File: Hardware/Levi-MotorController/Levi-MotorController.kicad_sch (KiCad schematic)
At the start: 3 parts

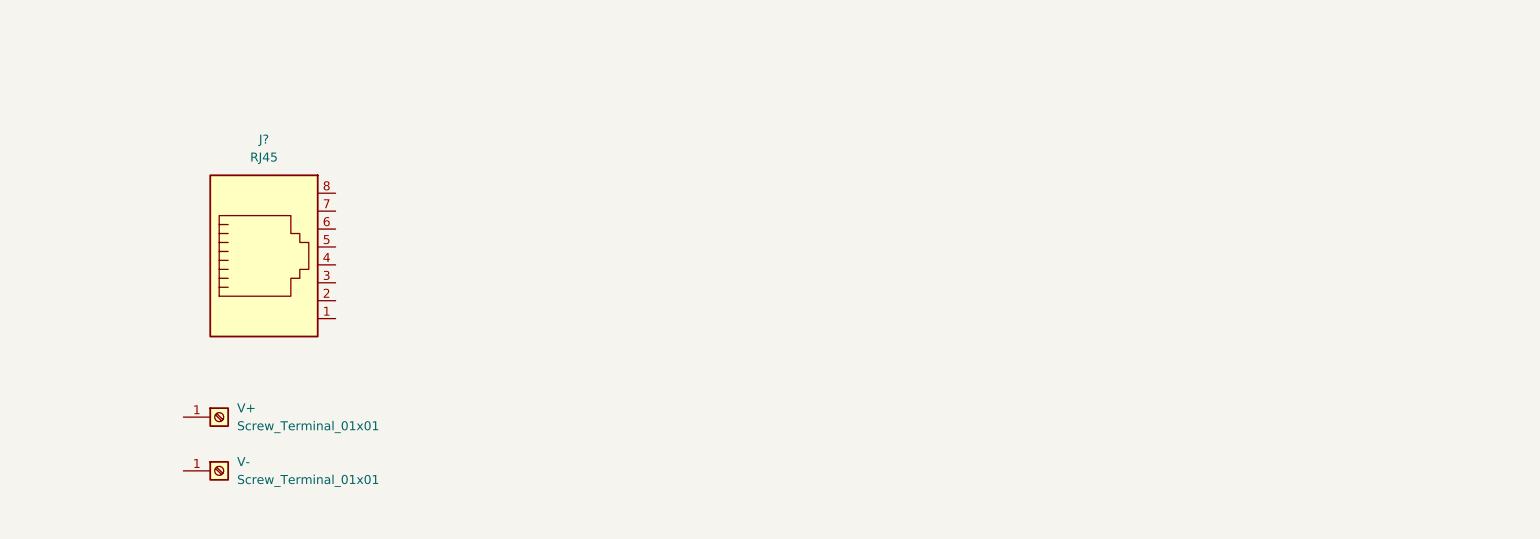
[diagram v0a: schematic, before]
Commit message: adding footprints
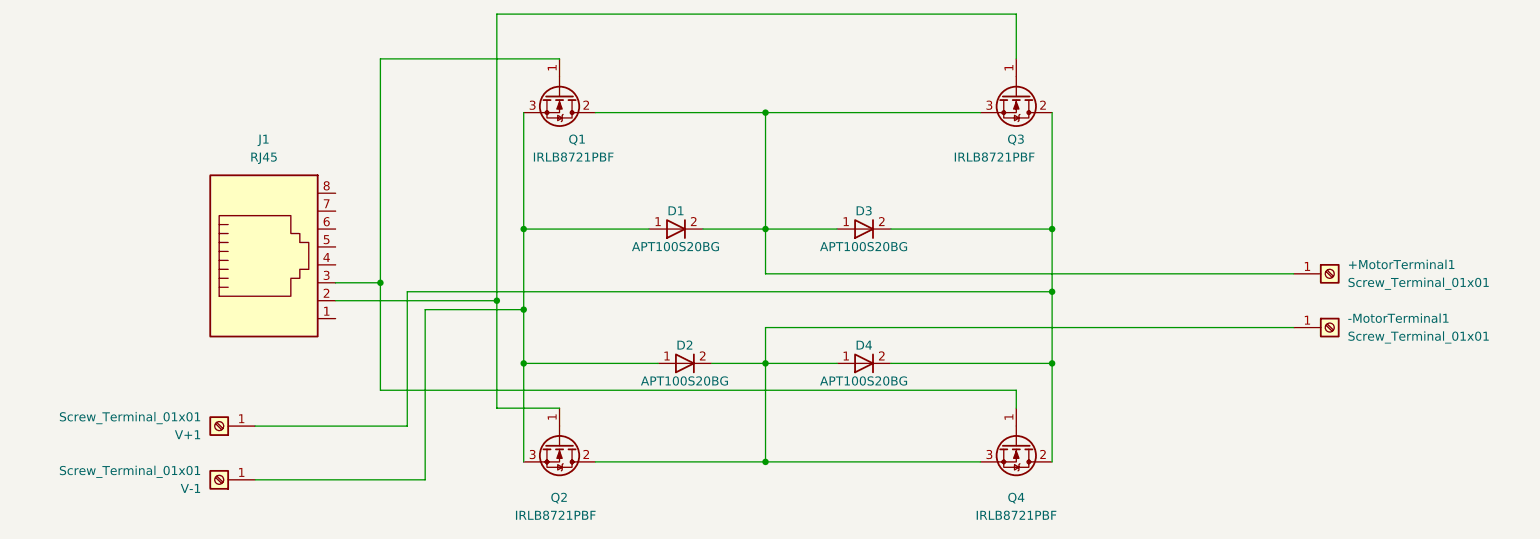
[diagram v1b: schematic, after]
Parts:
- added +MotorTerminal1, -MotorTerminal1: Screw_Terminal_01x01, TerminalBlock_Wuerth:Wuerth_REDCUBE-THR_WP-THRBU_74650195_THR, symbol Connector:Screw_Terminal_01x01
- added D1, D2, D3, D4: APT100S20BG, Schotty-Diode-THT:APT100S20BG, symbol Schotty-Diode-THT:APT100S20BG
- added Q1, Q2, Q3, Q4: IRLB8721PBF, Package_TO_SOT_THT:TO-220-3_Horizontal_TabUp, symbol Transistor_FET:IRLB8721PBF
- J1: renamed from J?; footprint (none) -> Connector_RJ:RJ45_Amphenol_RJHSE538X
- renumbered V+ to V+1, V- to V-1
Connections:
- net at V-1.1 (Pin_1): now also D1.1, D2.1, Q1.3 (S), Q2.3 (S)
- net at V+1.1 (Pin_1): now also D3.2, D4.2, Q3.2 (D), Q4.2 (D)
- net at J1.2: now also Q2.1 (G), Q3.1 (G)
- net at J1.3: now also Q1.1 (G), Q4.1 (G)
- new net: -MotorTerminal1.1 (Pin_1), D2.2, D4.1, Q2.2 (D), Q4.3 (S)
- new net: +MotorTerminal1.1 (Pin_1), D1.2, D3.1, Q1.2 (D), Q3.3 (S)
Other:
- moved on the sheet: V+1, V-1

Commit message: Added prototype motor controller
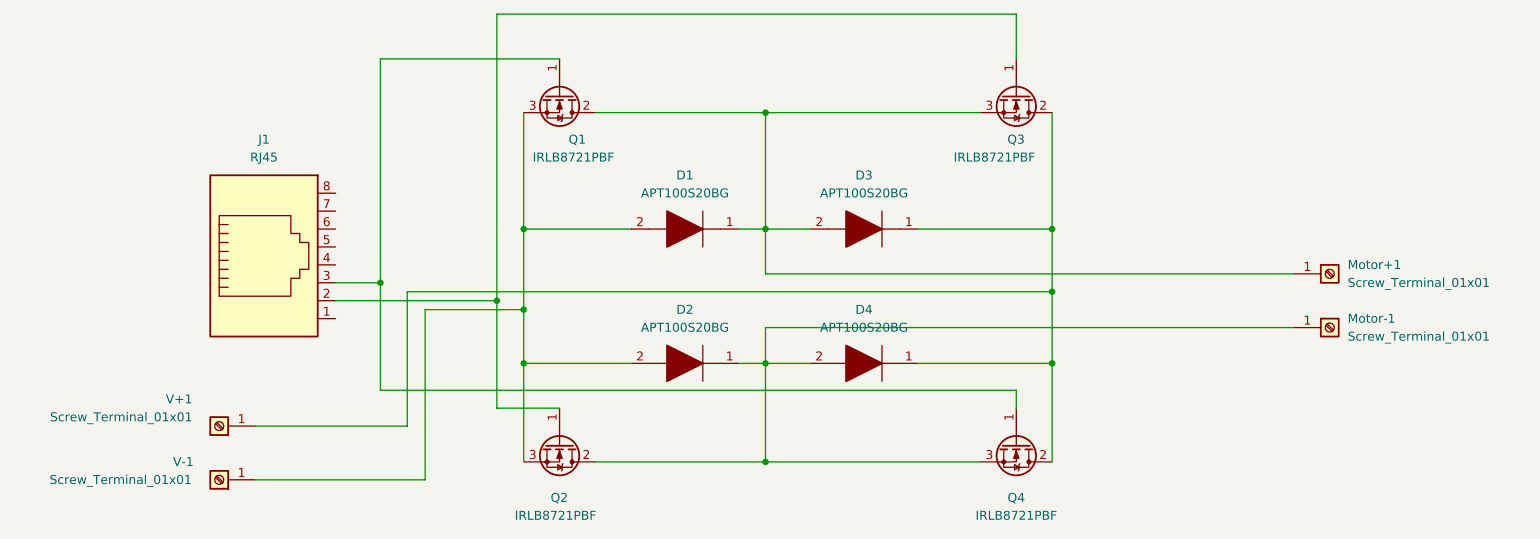
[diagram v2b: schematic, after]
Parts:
- removed +MotorTerminal1, -MotorTerminal1: Screw_Terminal_01x01, TerminalBlock_Wuerth:Wuerth_REDCUBE-THR_WP-THRBU_74650195_THR, symbol Connector:Screw_Terminal_01x01
- removed D1, D2, D3, D4: APT100S20BG, Schotty-Diode-THT:APT100S20BG, symbol Schotty-Diode-THT:APT100S20BG
- added D1, D2, D3, D4: APT100S20BG, TO1087P531X1588X2596-2P, symbol APT100S20BG:APT100S20BG
- added Motor+1, Motor-1: Screw_Terminal_01x01, Project_TerminalBlock_Wuerth:Wuerth_REDCUBE-THR_WP-THRSH_74651195_THR, symbol Connector:Screw_Terminal_01x01
- V+1, V-1: footprint TerminalBlock_Wuerth:Wuerth_REDCUBE-THR_WP-THRBU_74650195_THR -> Project_TerminalBlock_Wuerth:Wuerth_REDCUBE-THR_WP-THRSH_74651195_THR
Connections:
- net at Q1.3 (S), Q2.3 (S), V-1.1 (Pin_1): now also D1.2, D2.2
- net at Q2.2 (D), Q4.3 (S): now also D2.1, D4.2, Motor-1.1 (Pin_1)
- net at Q3.2 (D), Q4.2 (D), V+1.1 (Pin_1): now also D3.1, D4.1
- net at Q1.2 (D), Q3.3 (S): now also D1.1, D3.2, Motor+1.1 (Pin_1)
